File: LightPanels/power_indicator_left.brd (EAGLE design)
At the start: 48 x 47.5 mm, 23 parts, among them IC1 7805DT

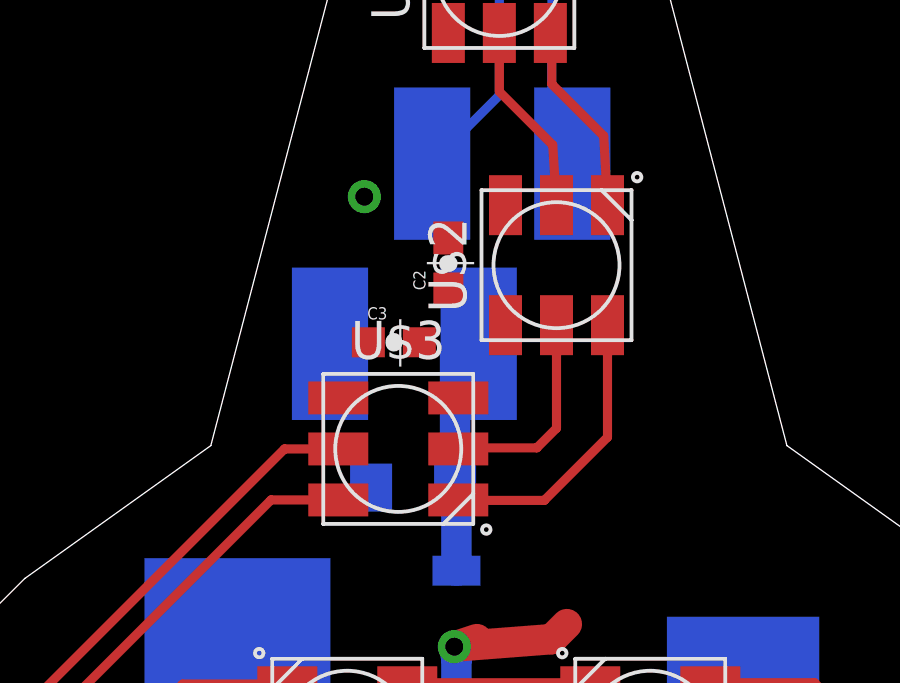
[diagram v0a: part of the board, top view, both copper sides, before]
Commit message: Power indicators more or less done
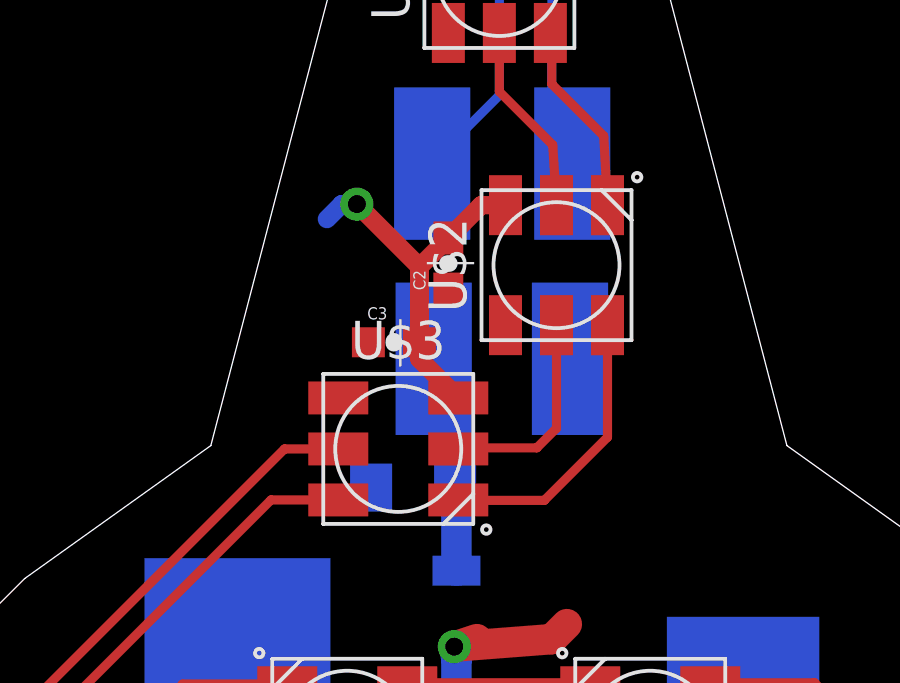
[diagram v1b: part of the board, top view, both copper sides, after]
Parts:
- moved GND 8.02 mm to (26.6, 24.3)
- moved +12V 1.58 mm to (22.1, 24.3)
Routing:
- net GND: track 25.5 -> 40.8 mm
- net +12V: track 8.18 -> 7.38 mm
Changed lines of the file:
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@@
 <attribute name="PROD_ID" value="CAP-08390" x="92.625" y="0.84" size="1.778" layer="27" rot="R180" display="off"/>
 </element>
-<element name="GND" library="wirepad" package="SMD2,54-5,08" value="WIREPADSMD2,54-5,08" x="18.605" y="24.845" rot="MR0"/>
-<element name="+12V" library="wirepad" package="SMD2,54-5,08" value="WIREPADSMD2,54-5,08" x="23.56" y="24.845" rot="MR0"/>
+<element name="GND" library="wirepad" package="SMD2,54-5,08" value="WIREPADSMD2,54-5,08" x="26.605" y="24.345" rot="MR0"/>
+<element name="+12V" library="wirepad" package="SMD2,54-5,08" value="WIREPADSMD2,54-5,08" x="22.06" y="24.345" rot="MR0"/>
 <element name="DI" library="wirepad" package="SMD2,54-5,08" value="WIREPADSMD2,54-5,08" x="26.68" y="30.85" rot="MR0"/>
 <element name="CI" library="wirepad" package="SMD2,54-5,08" value="WIREPADSMD2,54-5,08" x="22.01" y="30.85" rot="MR0"/>
@@
 <wire x1="36.875" y1="6.125" x2="36.875" y2="7.14" width="0.6096" layer="1"/>
 <wire x1="36.875" y1="7.14" x2="37.255" y2="7.645" width="0.6096" layer="1"/>
-<via x="19.75" y="29.75" extent="1-16" drill="0.6"/>
 <wire x1="22.55" y1="39.205" x2="22.55" y2="41.93" width="0.6096" layer="1"/>
 <wire x1="22.55" y1="41.93" x2="22.64" y2="42.52" width="0.6096" layer="1"/>
@@
 <wire x1="17.18" y1="10.145" x2="17.18" y2="8.68" width="0.6096" layer="1"/>
 <wire x1="17.18" y1="8.68" x2="17" y2="8.5" width="0.6096" layer="1"/>
-<wire x1="22.55" y1="28.37" x2="24.455" y2="29.465" width="0" layer="19" extent="1-1"/>
-<wire x1="19.75" y1="29.75" x2="22.55" y2="28.37" width="0" layer="19" extent="1-1"/>
-<wire x1="21.585" y1="24.895" x2="18.605" y2="24.845" width="0" layer="19" extent="1-16"/>
-<wire x1="22.88" y1="23.04" x2="21.585" y2="24.895" width="0" layer="19" extent="1-1"/>
+<wire x1="21.585" y1="24.895" x2="21.585" y2="24.335" width="0.6096" layer="1"/>
+<wire x1="21.585" y1="24.335" x2="22.88" y2="23.04" width="0.6096" layer="1"/>
+<wire x1="21.585" y1="24.895" x2="21.585" y2="27.405" width="0.6096" layer="1"/>
+<wire x1="21.585" y1="27.405" x2="22.55" y2="28.37" width="0.6096" layer="1"/>
+<wire x1="24.455" y1="29.465" x2="23.645" y2="29.465" width="0.6096" layer="1"/>
+<wire x1="23.645" y1="29.465" x2="22.55" y2="28.37" width="0.6096" layer="1"/>
+<wire x1="21.585" y1="24.895" x2="21.585" y2="27.415" width="0.6096" layer="1"/>
+<wire x1="21.585" y1="27.415" x2="19.5" y2="29.5" width="0.6096" layer="1"/>
+<via x="19.5" y="29.5" extent="1-16" drill="0.6"/>
+<wire x1="19.5" y1="29.5" x2="19" y2="29.5" width="0.6096" layer="16"/>
+<wire x1="19" y1="29.5" x2="18.5" y2="29" width="0.6096" layer="16"/>
 </signal>
 <signal name="+5V">
@@
 <wire x1="22.82" y1="17.28" x2="22.82" y2="20.005" width="1.016" layer="16"/>
 <wire x1="22.82" y1="20.005" x2="22.775" y2="20.05" width="1.016" layer="16"/>
-<wire x1="22.775" y1="20.05" x2="22.775" y2="24.63" width="1.016" layer="16"/>
-<wire x1="22.775" y1="24.63" x2="23.56" y2="24.845" width="1.016" layer="16"/>
+<wire x1="22.775" y1="20.05" x2="22.775" y2="23.63" width="1.016" layer="16"/>
+<wire x1="22.775" y1="23.63" x2="22.06" y2="24.345" width="1.016" layer="16"/>
 </signal>
 </signals>

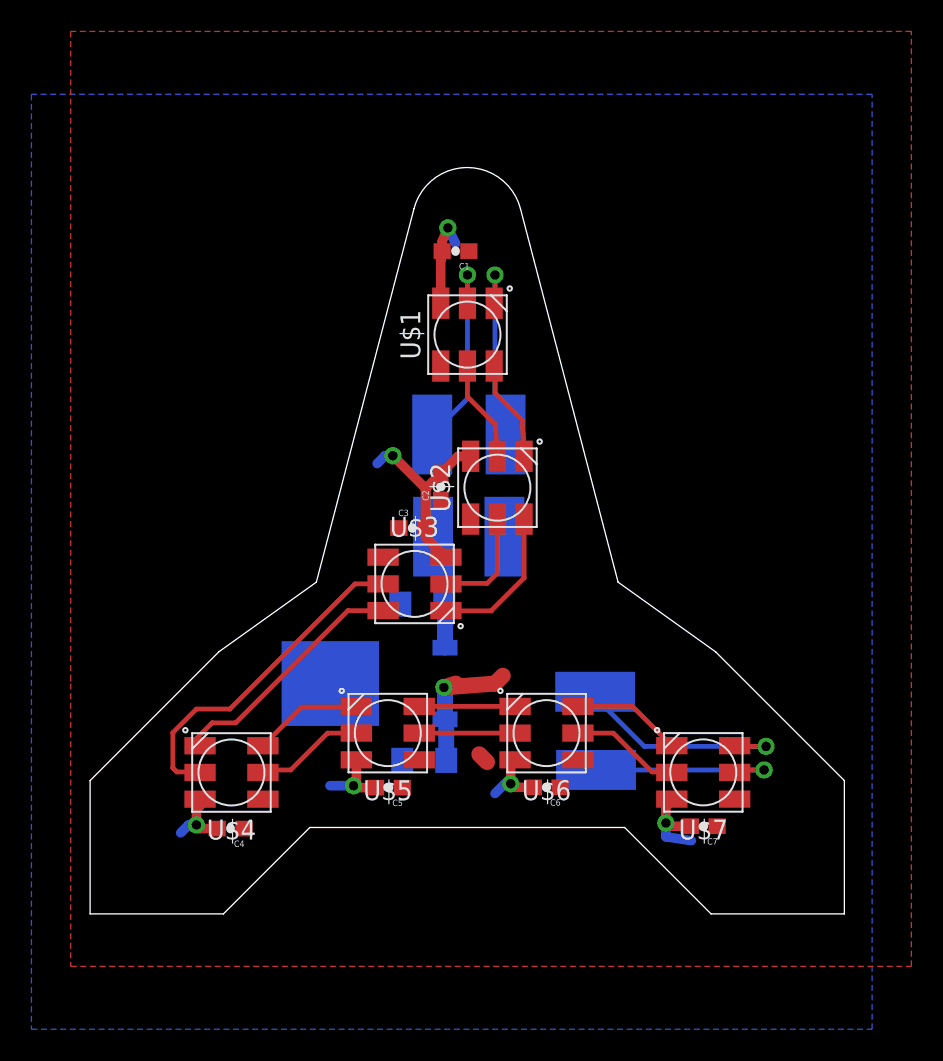
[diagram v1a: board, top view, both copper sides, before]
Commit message: Clean up light panels. Remvoe names/values
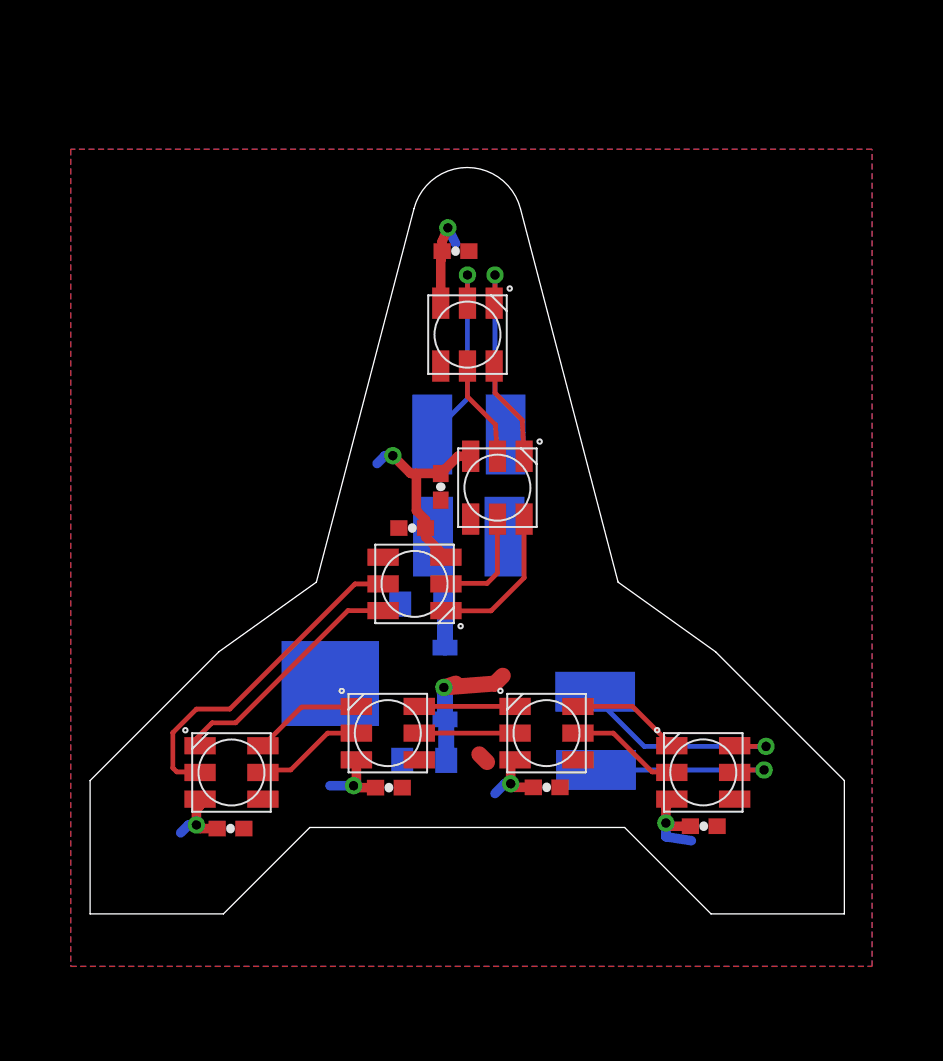
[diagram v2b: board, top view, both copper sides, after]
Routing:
- net GND: track 40.8 -> 38.7 mm
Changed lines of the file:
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@@
 </autorouter>
 <elements>
-<element name="U$1" library="jos-ph" package="APA102_5050" value="APA1025050" x="24.25" y="37.205" rot="R270"/>
-<element name="C1" library="SparkFun-Capacitors" package="0603-CAP" value="0.1uF" x="23.49" y="42.52" rot="R180">
+<element name="U$1" library="jos-ph" package="APA102_5050" value="APA1025050" x="24.25" y="37.205" smashed="yes" rot="R270"/>
+<element name="C1" library="SparkFun-Capacitors" package="0603-CAP" value="0.1uF" x="23.49" y="42.52" smashed="yes" rot="R180">
 <attribute name="PROD_ID" value="CAP-08390" x="36.19" y="20.93" size="1.778" layer="27" rot="R180" display="off"/>
+<attribute name="VALUE" x="24.506" y="43.663" size="0.4064" layer="27" font="vector" rot="R180"/>
 </element>
-<element name="U$2" library="jos-ph" package="APA102_5050" value="APA1025050" x="26.155" y="27.465" rot="R270"/>
-<element name="C2" library="SparkFun-Capacitors" package="0603-CAP" value="0.1uF" x="22.55" y="27.52" rot="R90">
+<element name="U$2" library="jos-ph" package="APA102_5050" value="APA1025050" x="26.155" y="27.465" smashed="yes" rot="R270"/>
+<element name="C2" library="SparkFun-Capacitors" package="0603-CAP" value="0.1uF" x="22.55" y="27.52" smashed="yes" rot="R90">
 <attribute name="PROD_ID" value="CAP-08390" x="4.77" y="3.39" size="1.778" layer="27" rot="R90" display="off"/>
+<attribute name="VALUE" x="23.693" y="26.504" size="0.4064" layer="27" font="vector" rot="R90"/>
 </element>
-<element name="U$3" library="jos-ph" package="APA102_5050" value="APA1025050" x="20.88" y="21.34" rot="R180"/>
-<element name="C3" library="SparkFun-Capacitors" package="0603-CAP" value="0.1uF" x="20.735" y="24.895">
+<element name="U$3" library="jos-ph" package="APA102_5050" value="APA1025050" x="20.88" y="21.34" smashed="yes" rot="R180"/>
+<element name="C3" library="SparkFun-Capacitors" package="0603-CAP" value="0.1uF" x="20.735" y="24.895" smashed="yes">
 <attribute name="PROD_ID" value="CAP-08390" x="-14.825" y="38.865" size="1.778" layer="27" display="off"/>
+<attribute name="VALUE" x="19.719" y="23.752" size="0.4064" layer="27" font="vector"/>
 </element>
-<element name="U$4" library="jos-ph" package="APA102_5050" value="APA1025050" x="9.23" y="9.34"/>
-<element name="C4" library="SparkFun-Capacitors" package="0603-CAP" value="0.1uF" x="9.17" y="5.77" rot="R180">
+<element name="U$4" library="jos-ph" package="APA102_5050" value="APA1025050" x="9.23" y="9.34" smashed="yes"/>
+<element name="C4" library="SparkFun-Capacitors" package="0603-CAP" value="0.1uF" x="9.17" y="5.77" smashed="yes" rot="R180">
 <attribute name="PROD_ID" value="CAP-08390" x="56.16" y="-4.39" size="1.778" layer="27" rot="R180" display="off"/>
+<attribute name="VALUE" x="10.186" y="6.913" size="0.4064" layer="27" font="vector" rot="R180"/>
 </element>
-<element name="U$5" library="jos-ph" package="APA102_5050" value="APA1025050" x="19.18" y="11.845"/>
-<element name="C5" library="SparkFun-Capacitors" package="0603-CAP" value="0.1uF" x="19.25" y="8.375" rot="R180">
+<element name="U$5" library="jos-ph" package="APA102_5050" value="APA1025050" x="19.18" y="11.845" smashed="yes"/>
+<element name="C5" library="SparkFun-Capacitors" package="0603-CAP" value="0.1uF" x="19.25" y="8.375" smashed="yes" rot="R180">
 <attribute name="PROD_ID" value="CAP-08390" x="77.67" y="2.025" size="1.778" layer="27" rot="R180" display="off"/>
+<attribute name="VALUE" x="20.266" y="9.518" size="0.4064" layer="27" font="vector" rot="R180"/>
 </element>
-<element name="U$6" library="jos-ph" package="APA102_5050" value="APA1025050" x="29.28" y="11.845"/>
-<element name="C6" library="SparkFun-Capacitors" package="0603-CAP" value="0.1uF" x="29.29" y="8.395" rot="R180">
+<element name="U$6" library="jos-ph" package="APA102_5050" value="APA1025050" x="29.28" y="11.845" smashed="yes"/>
+<element name="C6" library="SparkFun-Capacitors" package="0603-CAP" value="0.1uF" x="29.29" y="8.395" smashed="yes" rot="R180">
 <attribute name="PROD_ID" value="CAP-08390" x="99.14" y="5.855" size="1.778" layer="27" rot="R180" display="off"/>
+<attribute name="VALUE" x="30.306" y="9.538" size="0.4064" layer="27" font="vector" rot="R180"/>
 </element>
-<element name="U$7" library="jos-ph" package="APA102_5050" value="APA1025050" x="39.255" y="9.345"/>
-<element name="C7" library="SparkFun-Capacitors" package="0603-CAP" value="0.1uF" x="39.285" y="5.92" rot="R180">
+<element name="U$7" library="jos-ph" package="APA102_5050" value="APA1025050" x="39.255" y="9.345" smashed="yes"/>
+<element name="C7" library="SparkFun-Capacitors" package="0603-CAP" value="0.1uF" x="39.285" y="5.92" smashed="yes" rot="R180">
 <attribute name="PROD_ID" value="CAP-08390" x="92.625" y="0.84" size="1.778" layer="27" rot="R180" display="off"/>
+<attribute name="VALUE" x="40.301" y="7.063" size="0.4064" layer="27" font="vector" rot="R180"/>
 </element>
-<element name="GND" library="wirepad" package="SMD2,54-5,08" value="WIREPADSMD2,54-5,08" x="26.605" y="24.345" rot="MR0"/>
-<element name="+12V" library="wirepad" package="SMD2,54-5,08" value="WIREPADSMD2,54-5,08" x="22.06" y="24.345" rot="MR0"/>
-<element name="DI" library="wirepad" package="SMD2,54-5,08" value="WIREPADSMD2,54-5,08" x="26.68" y="30.85" rot="MR0"/>
-<element name="CI" library="wirepad" package="SMD2,54-5,08" value="WIREPADSMD2,54-5,08" x="22.01" y="30.85" rot="MR0"/>
-<element name="DO" library="wirepad" package="SMD2,54-5,08" value="WIREPADSMD2,54-5,08" x="32.375" y="14.475" rot="MR270"/>
-<element name="CO" library="wirepad" package="SMD2,54-5,08" value="WIREPADSMD2,54-5,08" x="32.43" y="9.5" rot="MR270"/>
-<element name="IC1" library="linear" package="TO252" value="7805DT" x="18.02" y="15" rot="MR270"/>
-<element name="C8" library="SparkFun-Retired" package="EIA3216" value="10uF" x="21.5" y="10.11" rot="MR180">
+<element name="GND" library="wirepad" package="SMD2,54-5,08" value="WIREPADSMD2,54-5,08" x="26.605" y="24.345" smashed="yes" rot="MR0">
+<attribute name="NAME" x="28.105" y="21.845" size="1.27" layer="26" rot="MR90"/>
+</element>
+<element name="+12V" library="wirepad" package="SMD2,54-5,08" value="WIREPADSMD2,54-5,08" x="22.06" y="24.345" smashed="yes" rot="MR0">
+<attribute name="NAME" x="23.56" y="21.845" size="1.27" layer="26" rot="MR90"/>
+</element>
+<element name="DI" library="wirepad" package="SMD2,54-5,08" value="WIREPADSMD2,54-5,08" x="26.68" y="30.85" smashed="yes" rot="MR0">
+<attribute name="NAME" x="28.18" y="28.35" size="1.27" layer="26" rot="MR90"/>
+</element>
+<element name="CI" library="wirepad" package="SMD2,54-5,08" value="WIREPADSMD2,54-5,08" x="22.01" y="30.85" smashed="yes" rot="MR0">
+<attribute name="NAME" x="23.51" y="28.35" size="1.27" layer="26" rot="MR90"/>
+</element>
+<element name="DO" library="wirepad" package="SMD2,54-5,08" value="WIREPADSMD2,54-5,08" x="32.375" y="14.475" smashed="yes" rot="MR270">
+<attribute name="NAME" x="34.875" y="15.975" size="1.27" layer="26" rot="MR0"/>
+</element>
+<element name="CO" library="wirepad" package="SMD2,54-5,08" value="WIREPADSMD2,54-5,08" x="32.43" y="9.5" smashed="yes" rot="MR270">
+<attribute name="NAME" x="34.93" y="11" size="1.27" layer="26" rot="MR0"/>
+</element>
+<element name="IC1" library="linear" package="TO252" value="7805DT" x="18.02" y="15" smashed="yes" rot="MR270"/>
+<element name="C8" library="SparkFun-Retired" package="EIA3216" value="10uF" x="21.5" y="10.11" smashed="yes" rot="MR180">
 <attribute name="PROD_ID" value="CAP-00811" x="21.5" y="10.11" size="1.778" layer="28" rot="MR180" display="off"/>
 </element>
-<element name="C9" library="SparkFun-Retired" package="EIA3216" value="10uF" x="21.375" y="20.05" rot="MR180">
+<element name="C9" library="SparkFun-Retired" package="EIA3216" value="10uF" x="21.375" y="20.05" smashed="yes" rot="MR180">
 <attribute name="PROD_ID" value="CAP-00811" x="21.375" y="20.05" size="1.778" layer="28" rot="MR180" display="off"/>
 </element>
@@
 <contactref element="C9" pad="C"/>
 <polygon width="0.3048" layer="16">
-<vertex x="-3.5" y="52.5"/>
-<vertex x="-3.5" y="-7"/>
-<vertex x="50" y="-7"/>
-<vertex x="50" y="52.5"/>
+<vertex x="-1" y="49"/>
+<vertex x="-1" y="-3"/>
+<vertex x="50" y="-3"/>
+<vertex x="50" y="49"/>
 </polygon>
 <wire x1="28.44" y1="8.395" x2="27.23" y2="8.395" width="0.6096" layer="1"/>
@@
 <wire x1="21.585" y1="24.895" x2="21.585" y2="24.335" width="0.6096" layer="1"/>
 <wire x1="21.585" y1="24.335" x2="22.88" y2="23.04" width="0.6096" layer="1"/>
-<wire x1="21.585" y1="24.895" x2="21.585" y2="27.405" width="0.6096" layer="1"/>
-<wire x1="21.585" y1="27.405" x2="22.55" y2="28.37" width="0.6096" layer="1"/>
 <wire x1="24.455" y1="29.465" x2="23.645" y2="29.465" width="0.6096" layer="1"/>
 <wire x1="23.645" y1="29.465" x2="22.55" y2="28.37" width="0.6096" layer="1"/>
-<wire x1="21.585" y1="24.895" x2="21.585" y2="27.415" width="0.6096" layer="1"/>
-<wire x1="21.585" y1="27.415" x2="19.5" y2="29.5" width="0.6096" layer="1"/>
 <via x="19.5" y="29.5" extent="1-16" drill="0.6"/>
 <wire x1="19.5" y1="29.5" x2="19" y2="29.5" width="0.6096" layer="16"/>
 <wire x1="19" y1="29.5" x2="18.5" y2="29" width="0.6096" layer="16"/>
+<wire x1="22.55" y1="28.37" x2="21" y2="28.37" width="0.6096" layer="1"/>
+<wire x1="21" y1="28.37" x2="20.63" y2="28.37" width="0.6096" layer="1"/>
+<wire x1="20.63" y1="28.37" x2="19.5" y2="29.5" width="0.6096" layer="1"/>
+<wire x1="21.585" y1="24.895" x2="21.585" y2="25.415" width="0.6096" layer="1"/>
+<wire x1="21.585" y1="25.415" x2="21" y2="26" width="0.6096" layer="1"/>
+<wire x1="21" y1="26" x2="21" y2="28.37" width="0.6096" layer="1"/>
 </signal>
 <signal name="+5V">
@@
 <contactref element="C8" pad="A"/>
 <polygon width="0.3048" layer="1">
-<vertex x="-1" y="15"/>
+<vertex x="-1" y="49"/>
 <vertex x="-1" y="-3"/>
-<vertex x="52.5" y="-3"/>
-<vertex x="52.5" y="56.5"/>
-<vertex x="-1" y="56.5"/>
-<vertex x="-1" y="15.5"/>
+<vertex x="50" y="-3"/>
+<vertex x="50" y="49"/>
 </polygon>
 <wire x1="25" y1="10.5" x2="25.5" y2="10" width="1.016" layer="1"/>
